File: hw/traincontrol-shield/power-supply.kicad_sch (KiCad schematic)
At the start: 9 parts, among them U1 MP2359DJ

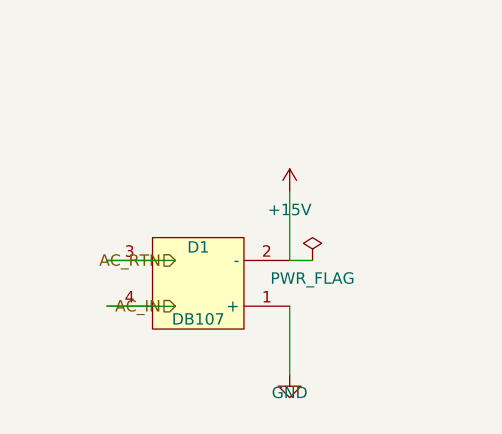
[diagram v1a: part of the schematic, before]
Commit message: Fix hlabel placement in power-supply sheet
Same lx→x fix applied to gen_power_supply.py's hlabel() function.
AC_IN and AC_RTN labels (angle=180, left-side inputs) now placed at
the circuit connection point instead of the stub tip.

Co-Authored-By: Claude Sonnet 4.6 <noreply@anthropic.com>
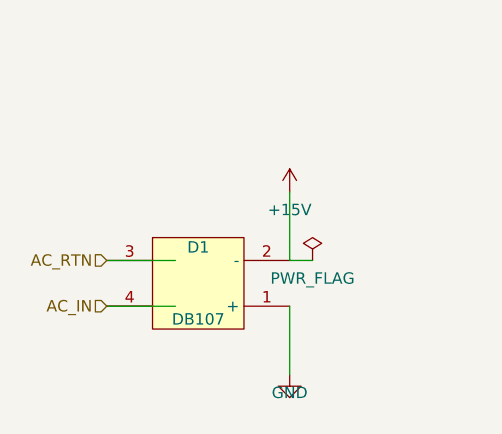
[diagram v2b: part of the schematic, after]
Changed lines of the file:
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@@
 	(hierarchical_label "AC_IN"
 		(shape input)
-		(at 48.26 71.12 180)
+		(at 40.64 71.12 180)
 		(fields_autoplaced yes)
 		(effects (font (size 1.27 1.27)) (justify right bottom))
 		(property "Intersheetrefs" "${INTERSHEET_REFS}"
-			(at 48.26 71.12 0)
+			(at 40.64 71.12 0)
 			(effects (font (size 1.27 1.27)) (hide yes))
 		)
@@
 	(hierarchical_label "AC_RTN"
 		(shape input)
-		(at 48.26 66.04 180)
+		(at 40.64 66.04 180)
 		(fields_autoplaced yes)
 		(effects (font (size 1.27 1.27)) (justify right bottom))
 		(property "Intersheetrefs" "${INTERSHEET_REFS}"
-			(at 48.26 66.04 0)
+			(at 40.64 66.04 0)
 			(effects (font (size 1.27 1.27)) (hide yes))
 		)

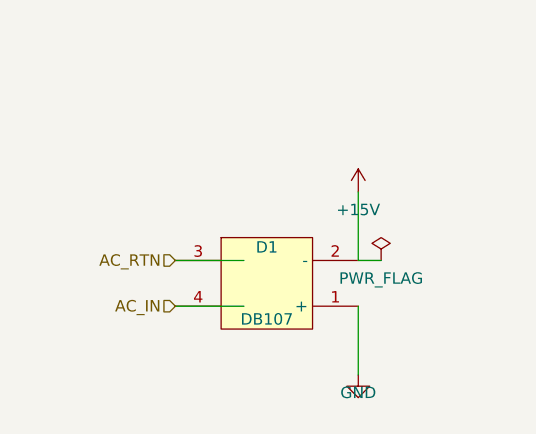
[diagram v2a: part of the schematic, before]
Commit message: Fix hlabel stub short-circuits on zero-crossing and power-supply pages
The hlabel() stub wire ran from the circuit pin inward, crossing directly
over series components and creating short-circuits:
- zero-crossing AC_IN: stub spanned R1 (x 81.28→88.90); shift x to 73.66
- power-supply AC_IN:  stub crossed D1 body (x 40.64→48.26); shift x to 33.02
- power-supply AC_RTN: same; shift x to 33.02

Pattern: for angle=180 labels, x = component_inner_pin - STUB so the
stub terminates at the component outer pin rather than spanning across it.

All 8 sheets validate with kicad-cli.

Co-Authored-By: Claude Sonnet 4.6 <noreply@anthropic.com>
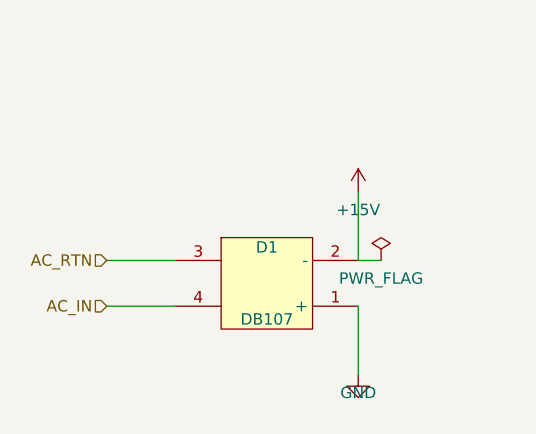
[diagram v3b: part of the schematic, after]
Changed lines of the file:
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@@
 	)
 	(wire
-		(pts (xy 40.64 71.12) (xy 48.26 71.12))
+		(pts (xy 33.02 71.12) (xy 40.64 71.12))
 		(stroke (width 0) (type solid))
 	)
 	(hierarchical_label "AC_IN"
 		(shape input)
-		(at 40.64 71.12 180)
+		(at 33.02 71.12 180)
 		(fields_autoplaced yes)
 		(effects (font (size 1.27 1.27)) (justify right bottom))
 		(property "Intersheetrefs" "${INTERSHEET_REFS}"
-			(at 40.64 71.12 0)
+			(at 33.02 71.12 0)
 			(effects (font (size 1.27 1.27)) (hide yes))
 		)
 	)
 	(wire
-		(pts (xy 40.64 66.04) (xy 48.26 66.04))
+		(pts (xy 33.02 66.04) (xy 40.64 66.04))
 		(stroke (width 0) (type solid))
 	)
 	(hierarchical_label "AC_RTN"
 		(shape input)
-		(at 40.64 66.04 180)
+		(at 33.02 66.04 180)
 		(fields_autoplaced yes)
 		(effects (font (size 1.27 1.27)) (justify right bottom))
 		(property "Intersheetrefs" "${INTERSHEET_REFS}"
-			(at 40.64 66.04 0)
+			(at 33.02 66.04 0)
 			(effects (font (size 1.27 1.27)) (hide yes))
 		)

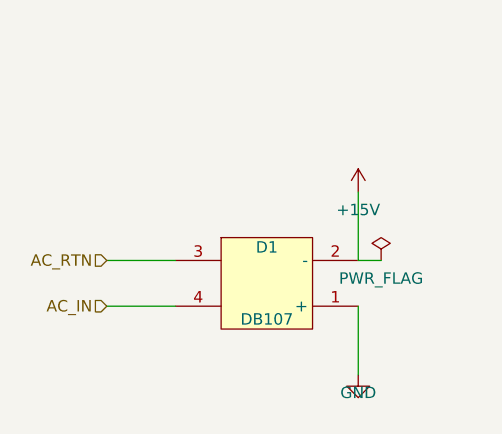
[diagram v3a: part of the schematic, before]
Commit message: Fix hlabel stub direction: stubs now extend away from IC, not into it
Root cause: hlabel() used dx = +STUB for angle=180 and -STUB for angle=0,
which caused every stub wire to run INTO the IC body instead of outward.
This made wires appear to connect at the inner (wrong) end of all pins.

Fix: negate dx so stubs always extend outward from the pin tip:
  angle=180 (left-side input):  dx = -STUB → stub extends LEFT  ✓
  angle=0   (right-side output): dx = +STUB → stub extends RIGHT ✓

Also revert the x-position workarounds that compensated for the wrong
stub direction (zero-crossing AC_IN, opto-triac PHASE/GATE, power-supply
AC_IN/RTN): these are now back at the actual component pin positions.

All 8 sheets validate with kicad-cli.

Co-Authored-By: Claude Sonnet 4.6 <noreply@anthropic.com>
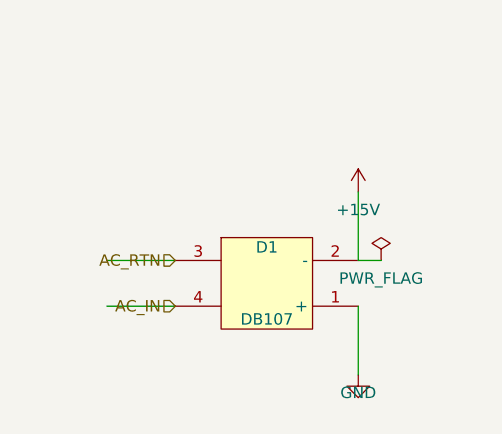
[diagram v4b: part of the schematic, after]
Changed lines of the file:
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@@
 	(hierarchical_label "AC_IN"
 		(shape input)
-		(at 33.02 71.12 180)
+		(at 40.64 71.12 180)
 		(fields_autoplaced yes)
 		(effects (font (size 1.27 1.27)) (justify right bottom))
 		(property "Intersheetrefs" "${INTERSHEET_REFS}"
-			(at 33.02 71.12 0)
+			(at 40.64 71.12 0)
 			(effects (font (size 1.27 1.27)) (hide yes))
 		)
@@
 	(hierarchical_label "AC_RTN"
 		(shape input)
-		(at 33.02 66.04 180)
+		(at 40.64 66.04 180)
 		(fields_autoplaced yes)
 		(effects (font (size 1.27 1.27)) (justify right bottom))
 		(property "Intersheetrefs" "${INTERSHEET_REFS}"
-			(at 33.02 66.04 0)
+			(at 40.64 66.04 0)
 			(effects (font (size 1.27 1.27)) (hide yes))
 		)

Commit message: Fix hlabel placement: label sits at stub outer end (lx), not pin tip (x)
The hierarchical label connection point must be at lx (the outer end of
the stub wire), not at x (the IC pin tip). With the label at x, it was
overlapping the pin itself instead of sitting at the end of the routing
stub where it belongs.

  angle=180 (left-side): lx = x - STUB  → label to the left of pin ✓
  angle=0   (right-side): lx = x + STUB  → label to the right of pin ✓

Wire still runs x↔lx, connecting the IC pin to the label connection.
Updated gen_all_sheets.py and gen_power_supply.py.

Co-Authored-By: Claude Sonnet 4.6 <noreply@anthropic.com>
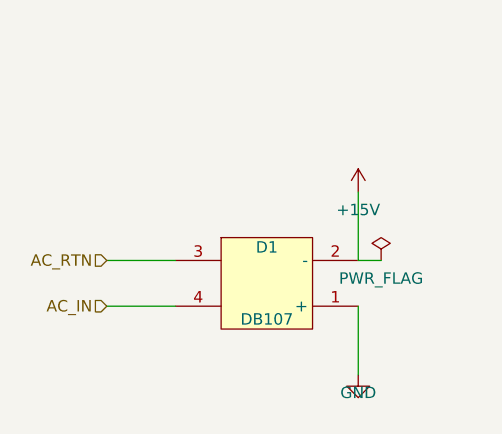
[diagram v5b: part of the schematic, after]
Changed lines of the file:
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@@
 	(hierarchical_label "AC_IN"
 		(shape input)
-		(at 40.64 71.12 180)
+		(at 33.02 71.12 180)
 		(fields_autoplaced yes)
 		(effects (font (size 1.27 1.27)) (justify right bottom))
 		(property "Intersheetrefs" "${INTERSHEET_REFS}"
-			(at 40.64 71.12 0)
+			(at 33.02 71.12 0)
 			(effects (font (size 1.27 1.27)) (hide yes))
 		)
@@
 	(hierarchical_label "AC_RTN"
 		(shape input)
-		(at 40.64 66.04 180)
+		(at 33.02 66.04 180)
 		(fields_autoplaced yes)
 		(effects (font (size 1.27 1.27)) (justify right bottom))
 		(property "Intersheetrefs" "${INTERSHEET_REFS}"
-			(at 40.64 66.04 0)
+			(at 33.02 66.04 0)
 			(effects (font (size 1.27 1.27)) (hide yes))
 		)

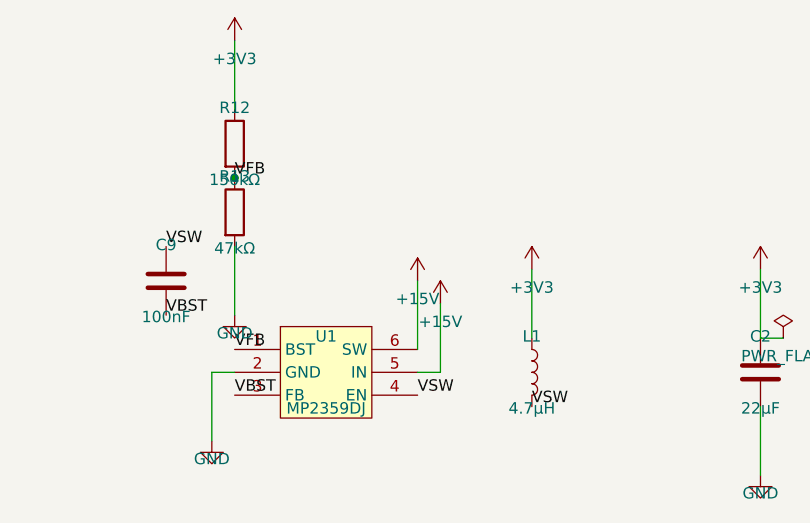
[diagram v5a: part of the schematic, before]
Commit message: Add wire stub to net_label, matching hlabel placement convention
net_label() now generates a short wire stub (length STUB) between the
component pin tip (x) and the label connection point (lx), placing the
label at the outer end of the stub — identical to how hlabel works:

  angle=180 (left-side):  lx = x - STUB, label left of pin  ✓
  angle=0   (right-side): lx = x + STUB, label right of pin ✓

Also fix XOR_OUT net labels at U4A/B left-side input pins (angle=0→180)
so their stubs extend leftward away from the IC body.

Updated gen_all_sheets.py and gen_power_supply.py.

Co-Authored-By: Claude Sonnet 4.6 <noreply@anthropic.com>
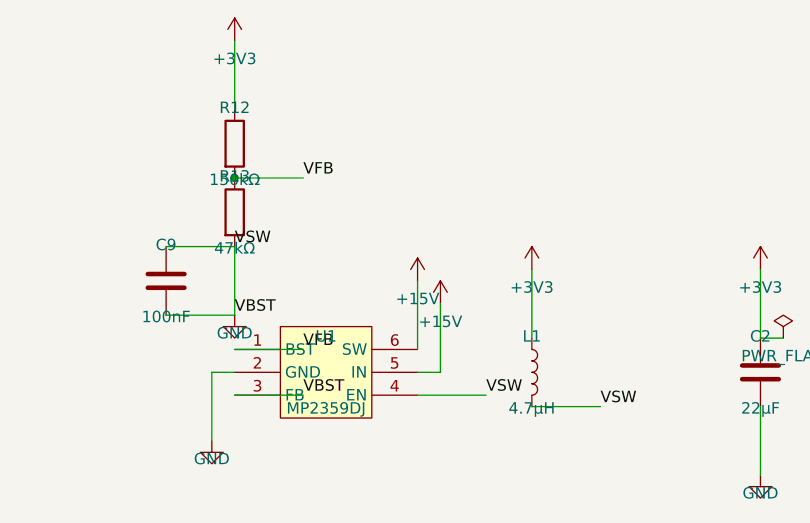
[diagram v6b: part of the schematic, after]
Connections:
- net VBST is gone; now on net GND: C9.2, U1.3 (FB)
- net VSW is gone; now on net GND: C9.1, L1.2, U1.4 (EN)
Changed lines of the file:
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@@
+		(stroke (width 0) (type solid))
+	)
+	(wire
+		(pts (xy 157.48 71.12) (xy 165.1 71.12))
 		(stroke (width 0) (type solid))
 	)
 	(label "VBST"
-		(at 157.48 71.12 0)
+		(at 165.1 71.12 0)
 		(fields_autoplaced yes)
 		(effects (font (size 1.27 1.27)) (justify left bottom))
 	)
+	(wire
+		(pts (xy 149.86 62.23) (xy 157.48000000000002 62.23))
+		(stroke (width 0) (type solid))
+	)
 	(label "VBST"
-		(at 149.86 62.23 0)
+		(at 157.48000000000002 62.23 0)
 		(fields_autoplaced yes)
 		(effects (font (size 1.27 1.27)) (justify left bottom))
 	)
+	(wire
+		(pts (xy 177.8 71.12) (xy 185.42000000000002 71.12))
+		(stroke (width 0) (type solid))
+	)
 	(label "VSW"
-		(at 177.8 71.12 0)
+		(at 185.42000000000002 71.12 0)
 		(fields_autoplaced yes)
 		(effects (font (size 1.27 1.27)) (justify left bottom))
 	)
+	(wire
+		(pts (xy 149.86 54.61) (xy 157.48000000000002 54.61))
+		(stroke (width 0) (type solid))
+	)
 	(label "VSW"
-		(at 149.86 54.61 0)
+		(at 157.48000000000002 54.61 0)
 		(fields_autoplaced yes)
 		(effects (font (size 1.27 1.27)) (justify left bottom))
 	)
+	(wire
+		(pts (xy 190.5 72.39) (xy 198.12 72.39))
+		(stroke (width 0) (type solid))
+	)
 	(label "VSW"
-		(at 190.5 72.39 0)
+		(at 198.12 72.39 0)
 		(fields_autoplaced yes)
 		(effects (font (size 1.27 1.27)) (justify left bottom))
 	)
+	(wire
+		(pts (xy 157.48 66.04) (xy 165.1 66.04))
+		(stroke (width 0) (type solid))
+	)
 	(label "VFB"
-		(at 157.48 66.04 0)
+		(at 165.1 66.04 0)
 		(fields_autoplaced yes)
 		(effects (font (size 1.27 1.27)) (justify left bottom))
 	)
+	(wire
+		(pts (xy 157.48 46.99) (xy 165.1 46.99))
+		(stroke (width 0) (type solid))
+	)
 	(label "VFB"
-		(at 157.48 46.99 0)
+		(at 165.1 46.99 0)
 		(fields_autoplaced yes)
 		(effects (font (size 1.27 1.27)) (justify left bottom))

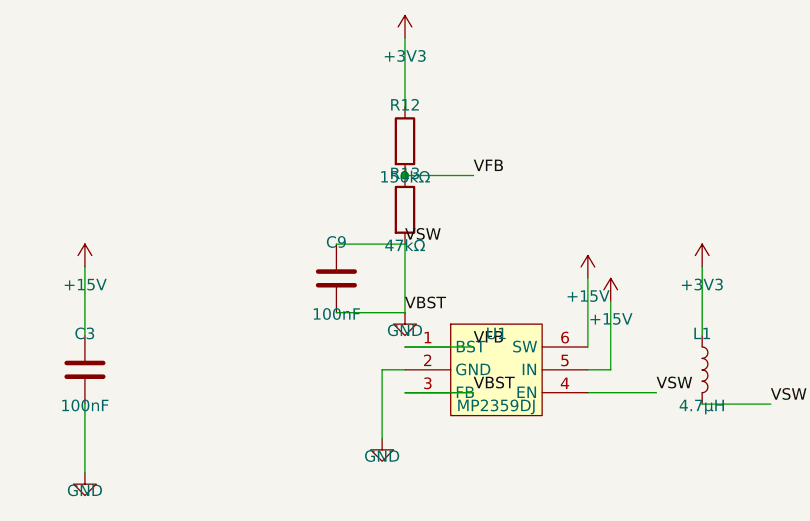
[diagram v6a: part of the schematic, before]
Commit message: Increase component spacing to eliminate pin-wire overlaps
- zero-crossing: move R1 left 7.62mm, add bridge wire to U2 pin2
- xor-interlock: move C10 right of U3 output (76→91mm), move C11 right (168→178mm)
- opto-triac: add 7.62mm COMP_GAP between MOC3021 and LED/gate resistors
- triacs-snubbers: move snubber column right (99→109mm), add 7.62mm gap between R and C
- mcu: widen C4/C5/C6 decap spacing from 7.62mm to 10.16mm
- power-supply: move R13 down 7.62mm, add bridge wire to R12

Co-Authored-By: Claude Sonnet 4.6 <noreply@anthropic.com>
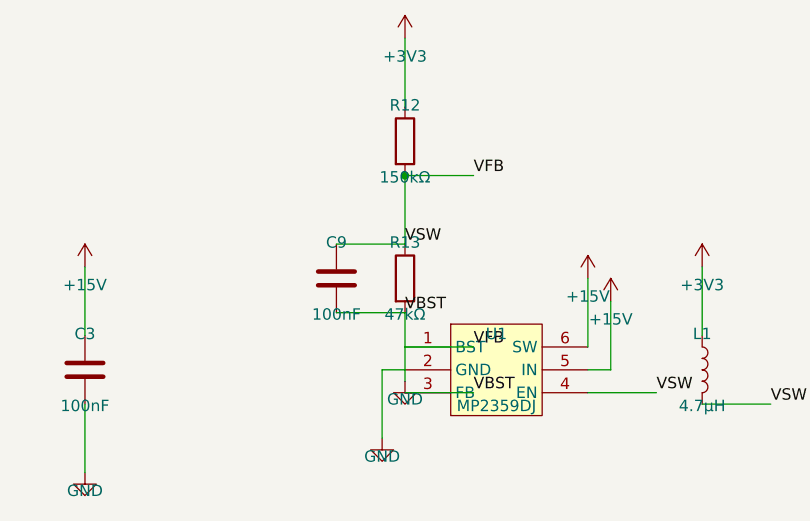
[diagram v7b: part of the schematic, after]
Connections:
- net GND: no longer C9.1, L1.2, U1.4 (EN)
- net VFB: now also C9.1, L1.2, U1.4 (EN)
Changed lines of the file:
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@@
 	(symbol
 		(lib_id "Device:R")
-		(at 157.48 50.8 0)
+		(at 157.48 58.42 0)
 		(unit 1)
 		(exclude_from_sim no)
@@
 		(dnp no)
 		(property "Reference" "R13"
-			(at 157.48 46.8 0)
+			(at 157.48 54.42 0)
 			(effects (font (size 1.27 1.27)))
 		)
 		(property "Value" "47kΩ"
-			(at 157.48 54.8 0)
+			(at 157.48 62.42 0)
 			(effects (font (size 1.27 1.27)))
 		)
 		(property "Footprint" "Resistor_SMD:R_0603_1608Metric"
-			(at 157.48 50.8 0)
+			(at 157.48 58.42 0)
 			(effects (font (size 1.27 1.27)) (hide yes))
 		)
 		(property "Datasheet" "~"
-			(at 157.48 50.8 0)
+			(at 157.48 58.42 0)
 			(effects (font (size 1.27 1.27)) (hide yes))
 		)
@@
 	)
 	(wire
-		(pts (xy 157.48 54.61) (xy 157.48 62.23))
+		(pts (xy 157.48 62.23) (xy 157.48 69.85))
 		(stroke (width 0) (type solid))
 	)
 	(symbol
 		(lib_id "power:GND")
-		(at 157.48 62.23 0)
+		(at 157.48 69.85 0)
 		(unit 1)
 		(exclude_from_sim no)
@@
 		(dnp no)
 		(property "Reference" "#PWR0214"
-			(at 157.48 60.23 0)
+			(at 157.48 67.85 0)
 			(effects (font (size 1.27 1.27)) (hide yes))
 		)
 		(property "Value" "GND"
-			(at 157.48 64.22999999999999 0)
-			(effects (font (size 1.27 1.27)))
-		)
-		(property "Footprint" ""
-			(at 157.48 62.23 0)
-			(effects (font (size 1.27 1.27)) (hide yes))
-		)
-		(property "Datasheet" ""
-			(at 157.48 62.23 0)
+			(at 157.48 71.85 0)
+			(effects (font (size 1.27 1.27)))
+		)
+		(property "Footprint" ""
+			(at 157.48 69.85 0)
+			(effects (font (size 1.27 1.27)) (hide yes))
+		)
+		(property "Datasheet" ""
+			(at 157.48 69.85 0)
 			(effects (font (size 1.27 1.27)) (hide yes))
 		)
@@
 	)
 	(wire
+		(pts (xy 157.48 46.99) (xy 157.48 54.61))
+		(stroke (width 0) (type solid))
+	)
+	(wire
